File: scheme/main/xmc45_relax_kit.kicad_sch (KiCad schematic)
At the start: 0 parts

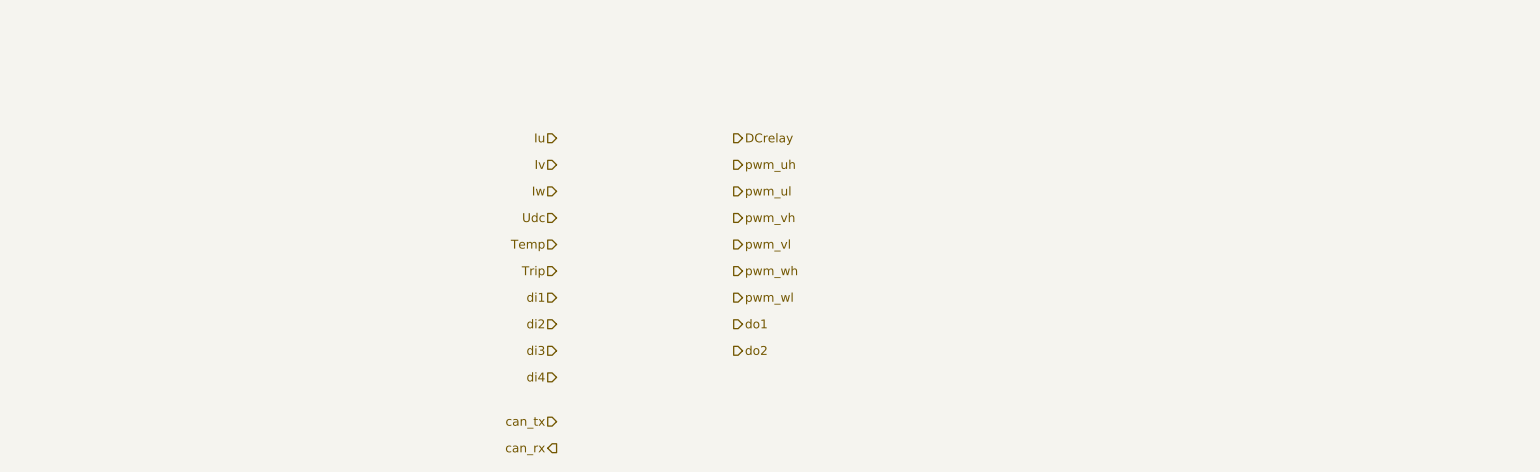
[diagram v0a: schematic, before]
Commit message: KIT_XMC47_RELAX_V1 symbol
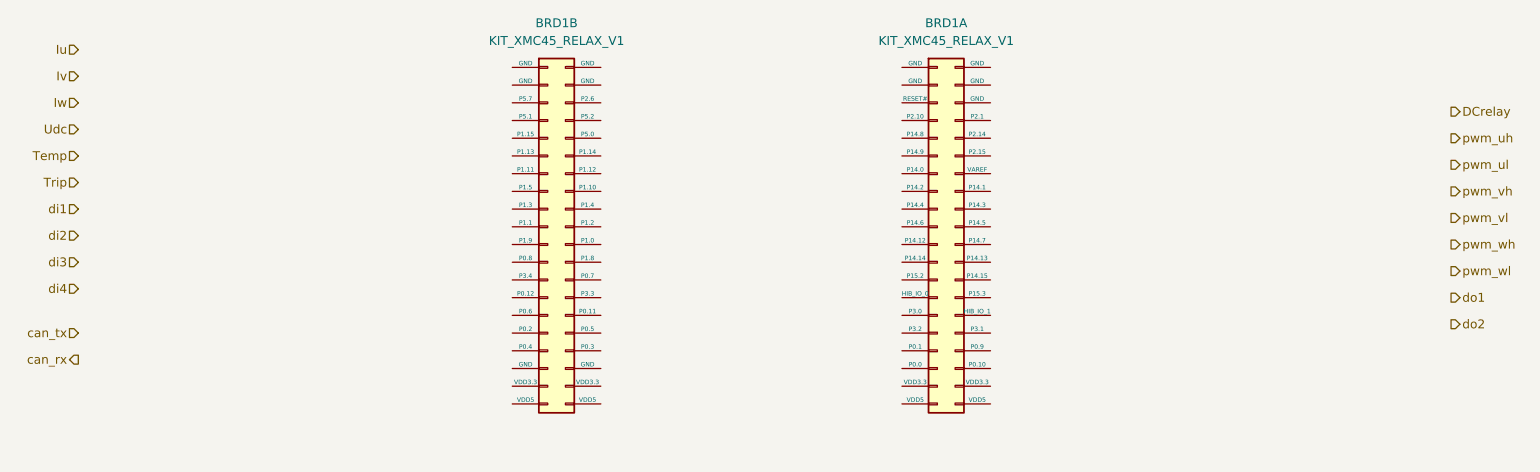
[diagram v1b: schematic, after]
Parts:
- added BRD1: KIT_XMC45_RELAX_V1, symbol main:KIT_XMC45_RELAX_V1
